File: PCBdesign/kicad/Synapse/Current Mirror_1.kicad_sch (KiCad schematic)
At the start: 5 parts, among them IC2 ALD1105PBL

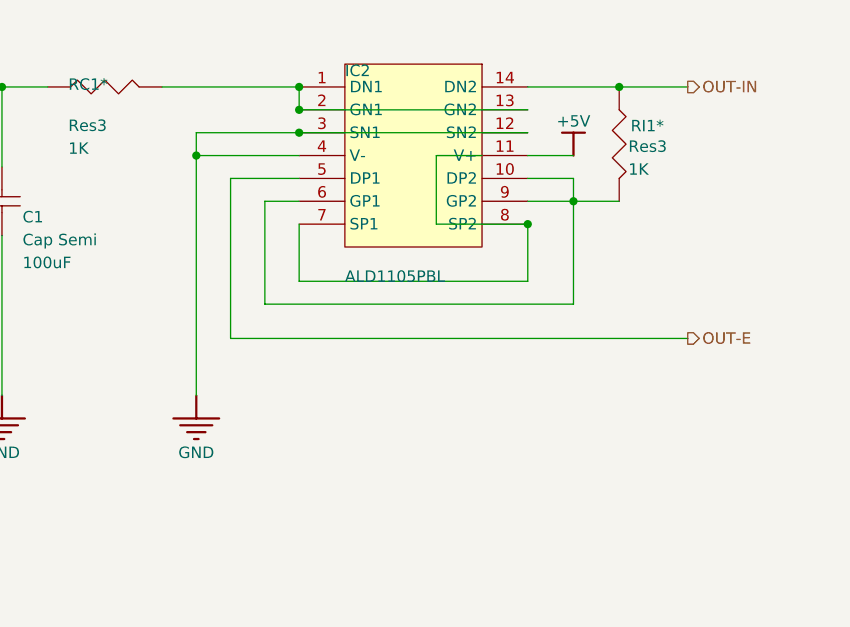
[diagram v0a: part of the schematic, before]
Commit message: update schematics for replacing ALD w/ discrete BJTs
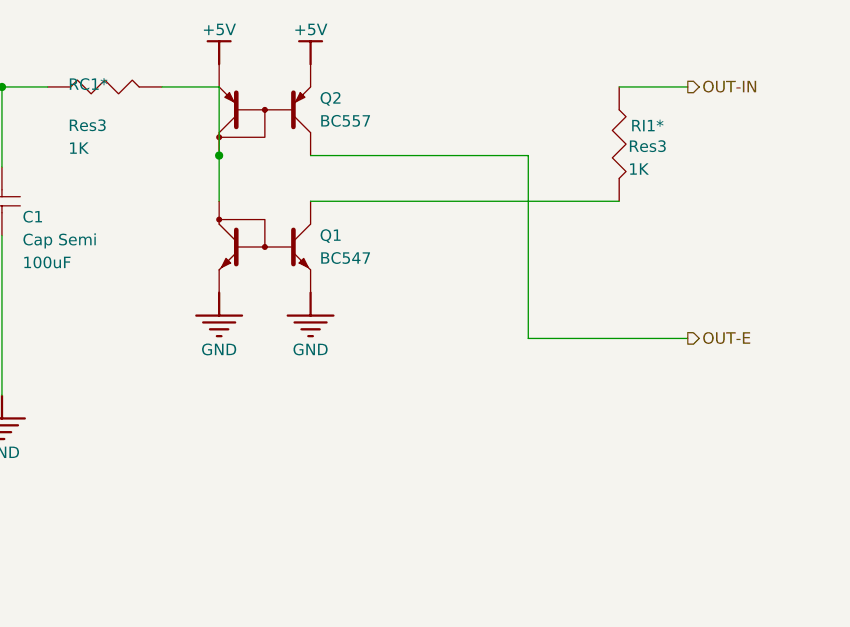
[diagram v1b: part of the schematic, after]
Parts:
- removed IC2: ALD1105PBL, C__Users_86135_Documents_AltiumLL_SamacSys.PcbLib:DIP762W51P254L1828H508Q14N, symbol *:1_0_ALD1105PBL_*
- added Q1: BC547, symbol Device:Q_NPN_CurrentMirror
- added Q2: BC557, symbol Device:Q_PNP_CurrentMirror
- C1: LATESTREVISIONDATE 29-May-2009 -> (none); LATESTREVISIONNOTE IPC-7351 Footprint Added. -> (none); PACKAGEDESCRIPTION Chip Capacitor -> (none); PACKAGEREFERENCE C1206 -> (none); PUBLISHED 8-Jun-2000 -> (none); PUBLISHER Altium Limited -> (none)
- C2: PACKAGEDESCRIPTION Capacitor; 2 Leads -> (none); PACKAGEREFERENCE CAPR5-4X5 -> (none); PUBLISHED 23-Sep-2002 -> (none); PUBLISHER Altium Limited -> (none)
- RC1*, RI1*: LATESTREVISIONDATE 29-May-2009 -> (none); LATESTREVISIONNOTE IPC-7351 Footprint Added. -> (none); PACKAGEDESCRIPTION Chip Resistor -> (none); PACKAGEREFERENCE J1-0603 -> (none); PUBLISHED 8-Jun-2000 -> (none); PUBLISHER Altium Limited -> (none)
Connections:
- net +5V: now also Q2.E1, Q2.E2
- net GND: now also Q1.E1, Q1.E2
- net OUT-E: now also Q2.C1
- net at RI1*.2: now also Q1.C1
- net at RC1*.2: now also Q1.C2, Q2.C2

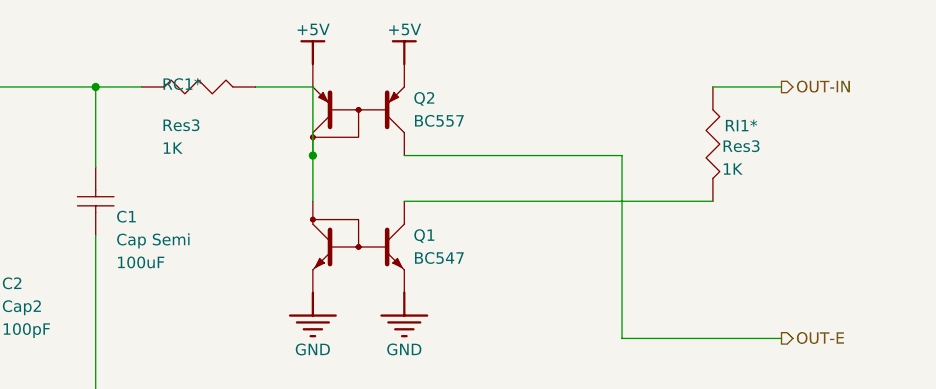
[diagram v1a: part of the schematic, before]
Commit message: Add annotation script, wiring checklist for breadboarding, and .gitignore in case proprietary libs are added. Fix annotations that were missing after KiCad import in the schematics.
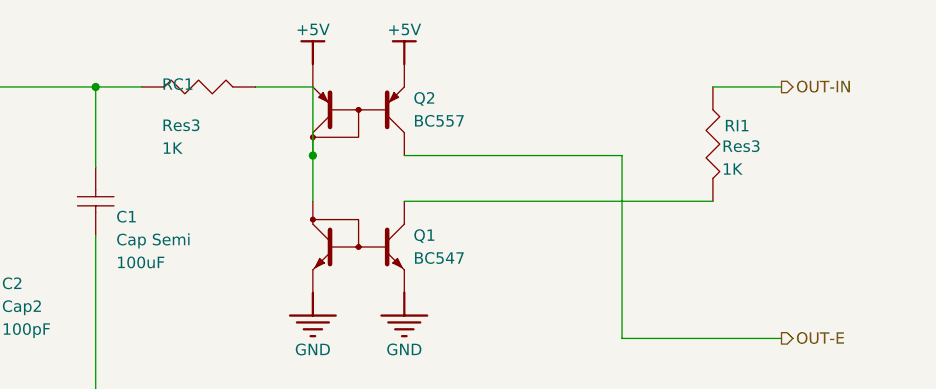
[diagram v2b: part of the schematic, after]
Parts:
- renumbered RC1* to RC1, RI1* to RI1
